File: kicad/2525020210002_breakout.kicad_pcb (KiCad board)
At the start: 2 copper layers, 40 x 30 mm, 17 parts, among them J1 I2C_IN, J2 I2C_OUT, J3 Conn_01x04_Socket, U1 2525020210002

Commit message: generated BOM, fixed fab layer error
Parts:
- J1: value I2C_IN -> JST_PH_B4B-PH-K
- J2: value I2C_OUT -> JST_PH_B4B-PH-K
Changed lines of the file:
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@@
     (property "Sheetfile" "2525020210002_breakout.kicad_sch")
     (property "Sheetname" "")
+    (property "exclude_from_bom" "")
     (property "ki_description" "Mounting Hole without connection")
     (property "ki_keywords" "mounting hole")
-    (attr exclude_from_pos_files)
+    (attr exclude_from_pos_files exclude_from_bom)
     (fp_text reference "H4" (at 0 -4.2) (layer "F.SilkS") hide
         (effects (font (size 1 1) (thickness 0.15)))
@@
         (effects (font (size 1 1) (thickness 0.16)))
     )
-    (fp_text value "I2C_IN" (at 3 3.6635 90) (layer "F.Fab")
+    (fp_text value "JST_PH_B4B-PH-K" (at 3.114 -3.452 90) (layer "F.Fab")
         (effects (font (size 1 1) (thickness 0.15)))
     )
@@
     (property "Sheetfile" "2525020210002_breakout.kicad_sch")
     (property "Sheetname" "")
+    (property "exclude_from_bom" "")
     (property "ki_description" "Mounting Hole without connection")
     (property "ki_keywords" "mounting hole")
-    (attr exclude_from_pos_files)
+    (attr exclude_from_pos_files exclude_from_bom)
     (fp_text reference "H2" (at 4.544 -0.336) (layer "F.SilkS") hide
         (effects (font (size 1 1) (thickness 0.15)))
@@
     (property "Sheetfile" "2525020210002_breakout.kicad_sch")
     (property "Sheetname" "")
+    (property "exclude_from_bom" "")
     (property "ki_description" "Mounting Hole without connection")
     (property "ki_keywords" "mounting hole")
-    (attr exclude_from_pos_files)
+    (attr exclude_from_pos_files exclude_from_bom)
     (fp_text reference "H3" (at 0 -4.2) (layer "F.SilkS") hide
         (effects (font (size 1 1) (thickness 0.15)))
@@
         (effects (font (size 1 1) (thickness 0.16)))
     )
-    (fp_text value "I2C_OUT" (at 3 4 90) (layer "F.Fab")
+    (fp_text value "JST_PH_B4B-PH-K" (at 3 4 90) (layer "F.Fab")
         (effects (font (size 1 1) (thickness 0.15)))
     )
@@
     (property "Sheetfile" "2525020210002_breakout.kicad_sch")
     (property "Sheetname" "")
+    (property "exclude_from_bom" "")
     (property "ki_description" "Mounting Hole without connection")
     (property "ki_keywords" "mounting hole")
-    (attr exclude_from_pos_files)
+    (attr exclude_from_pos_files exclude_from_bom)
     (fp_text reference "H1" (at 0 -4.2) (layer "F.SilkS") hide
         (effects (font (size 1 1) (thickness 0.15)))

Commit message: missing LED part no.
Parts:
- D1: value LED -> 150060VS7500
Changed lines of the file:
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@@
         (effects (font (size 1 1) (thickness 0.16)))
     )
-    (fp_text value "LED" (at -2.423061 0.056569 -45) (layer "F.Fab")
+    (fp_text value "150060VS7500" (at -1.546249 1.499066) (layer "F.Fab")
         (effects (font (size 1 1) (thickness 0.15)))
     )

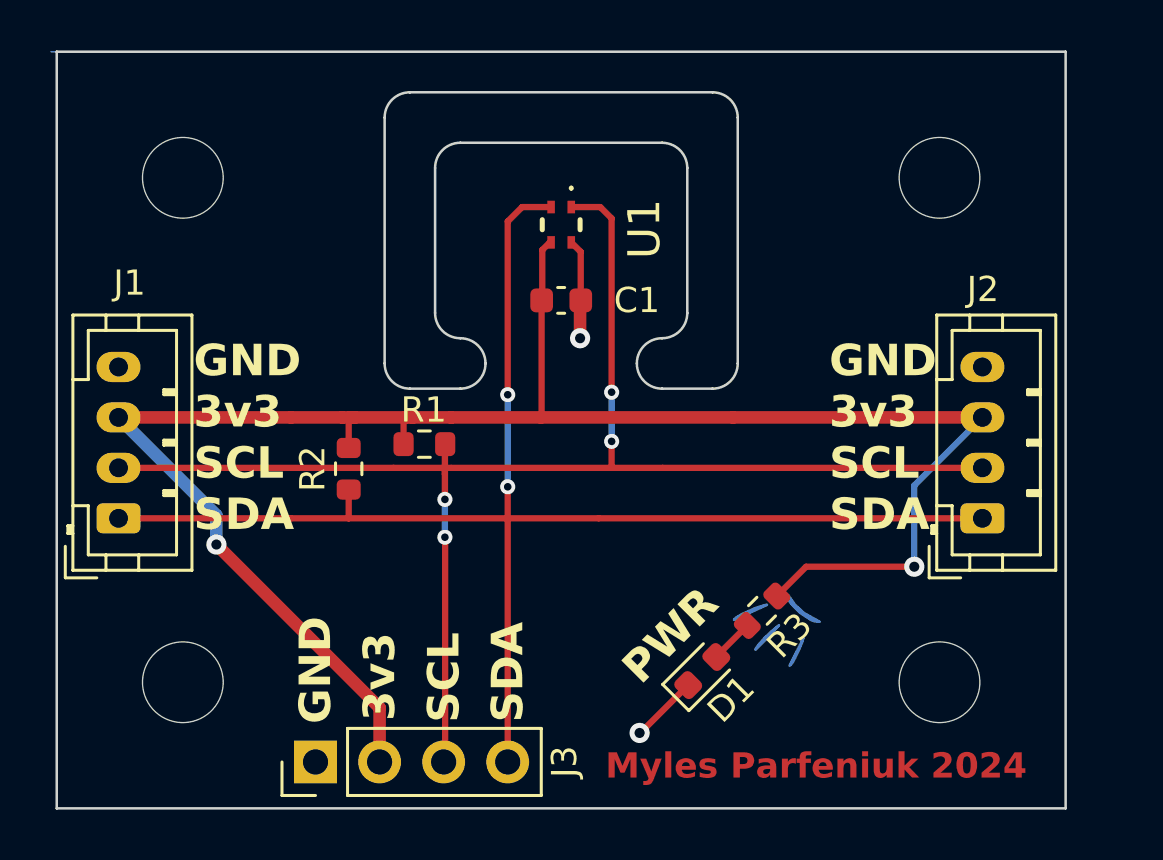
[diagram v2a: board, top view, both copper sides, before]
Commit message: Swapped SDA & SCL pins, rounded edgecuts
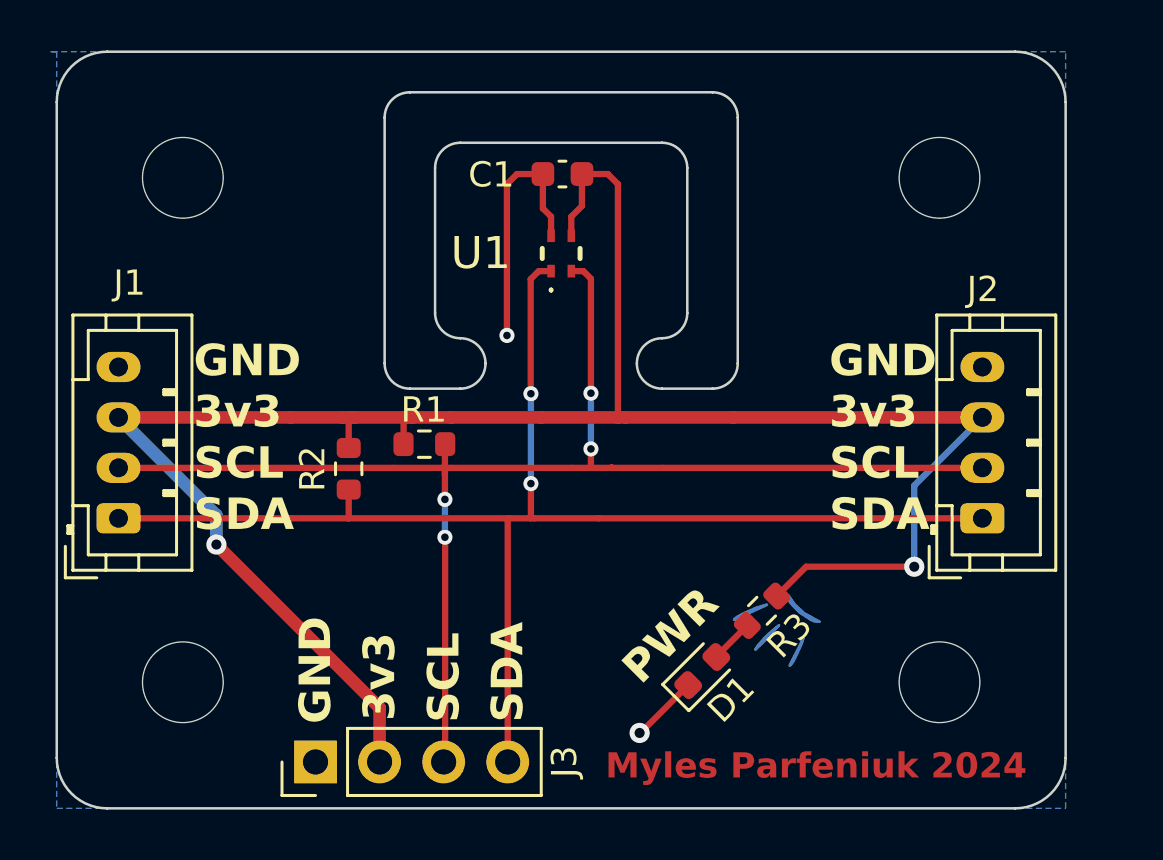
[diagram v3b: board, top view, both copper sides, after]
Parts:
- moved C1 5.01 mm to (140.3, 85.8), turned to 180 degrees
- moved U1 1.14 mm to (140.2, 89.0), turned to 90 degrees
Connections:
- U1 pad 1: /I2C1_SCL -> /I2C1_SDA
- U1 pad 2: /I2C1_SDA -> /I2C1_SCL
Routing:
- net +3V3: track 75.0 -> 81.4 mm
- net GND: track 6.68 -> 12.9 mm
- net /I2C1_SDA: track 59.0 -> 55.7 mm
- net /I2C1_SCL: track 59.1 -> 55.8 mm
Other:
- outline, holes or cut-outs redrawn
- board text added: "WSEN-HIDS Breakout Rev1.1"
- board text removed: "WSEN-HIDS Breakout Rev1.0"
